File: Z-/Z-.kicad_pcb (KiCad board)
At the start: 4 copper layers, 98 x 98 mm, 138 parts, among them J1 200528-0100, J2 Conn_Coaxial, J3 Conn_Coaxial, J4 200528-0100, J5 Conn_01x02, K1 IM02DGR, Q1 NX3008NBKS, Q10 NX3008NBKS, Q11 IRLML2803, Q12 MBT2222ADW1T1, Q13 IRLML2803, Q14 NX3008NBKS, Q15 IRF7404, Q16 MBT2222ADW1T1, Q17 IRF7404, Q18 IRLML2803, Q19 IRF7404, Q2 NX3008NBKS, Q3 MBT2222ADW1T1, Q4 MBT2222ADW1T1, Q5 NX3008NBKS, Q6 NX3008NBKS, Q7 MBT2222ADW1T1, Q8 MBT2222ADW1T1, Q9 MMBT2222AT, U1 OPT4003DNPRQ1, U2 LTC4316xDD, U3 ADM1176-1ARMZ-R7, U4 NCV891330PD50R2G, U5 DRV8830DRC

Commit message: Moved things around
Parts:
- moved Q15 98.6 mm to (206.3, 52.5)
- moved Q17 98.6 mm to (219.8, 52.5)
- moved Q11 98.6 mm to (204.4, 58.5)
- moved Q18 98.6 mm to (211.1, 58.5)
- moved Q19 98.6 mm to (213.0, 52.5)
- moved R56 98.6 mm to (214.4, 60.6)
- moved R59 98.6 mm to (214.4, 59.0)
- moved R60 98.6 mm to (214.4, 57.4)
- moved Q13 98.6 mm to (217.8, 58.5)
- moved R39 98.6 mm to (207.7, 60.6)
- moved R41 98.6 mm to (207.7, 59.0)
- moved R43 98.6 mm to (207.7, 57.3)
- moved R49 98.6 mm to (221.1, 60.6)
- moved R51 98.6 mm to (221.1, 59.0)
- moved R53 98.6 mm to (221.1, 57.4)
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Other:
- board text added: "SUN SENSOR"

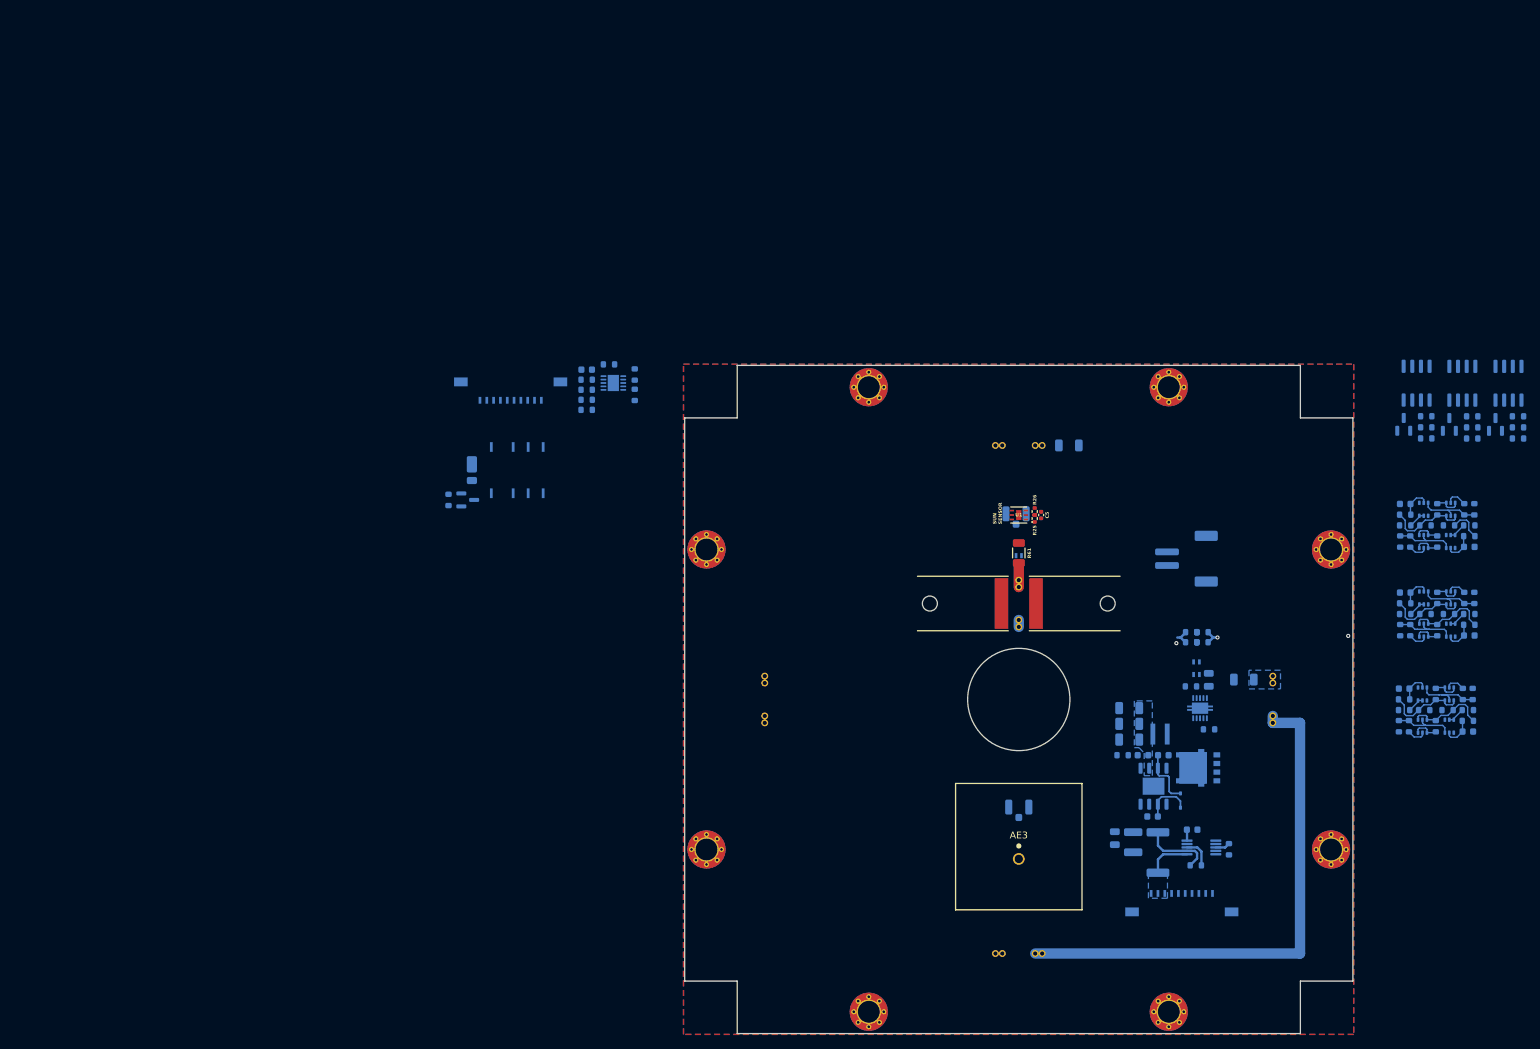
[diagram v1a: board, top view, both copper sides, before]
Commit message: Reworked board layout
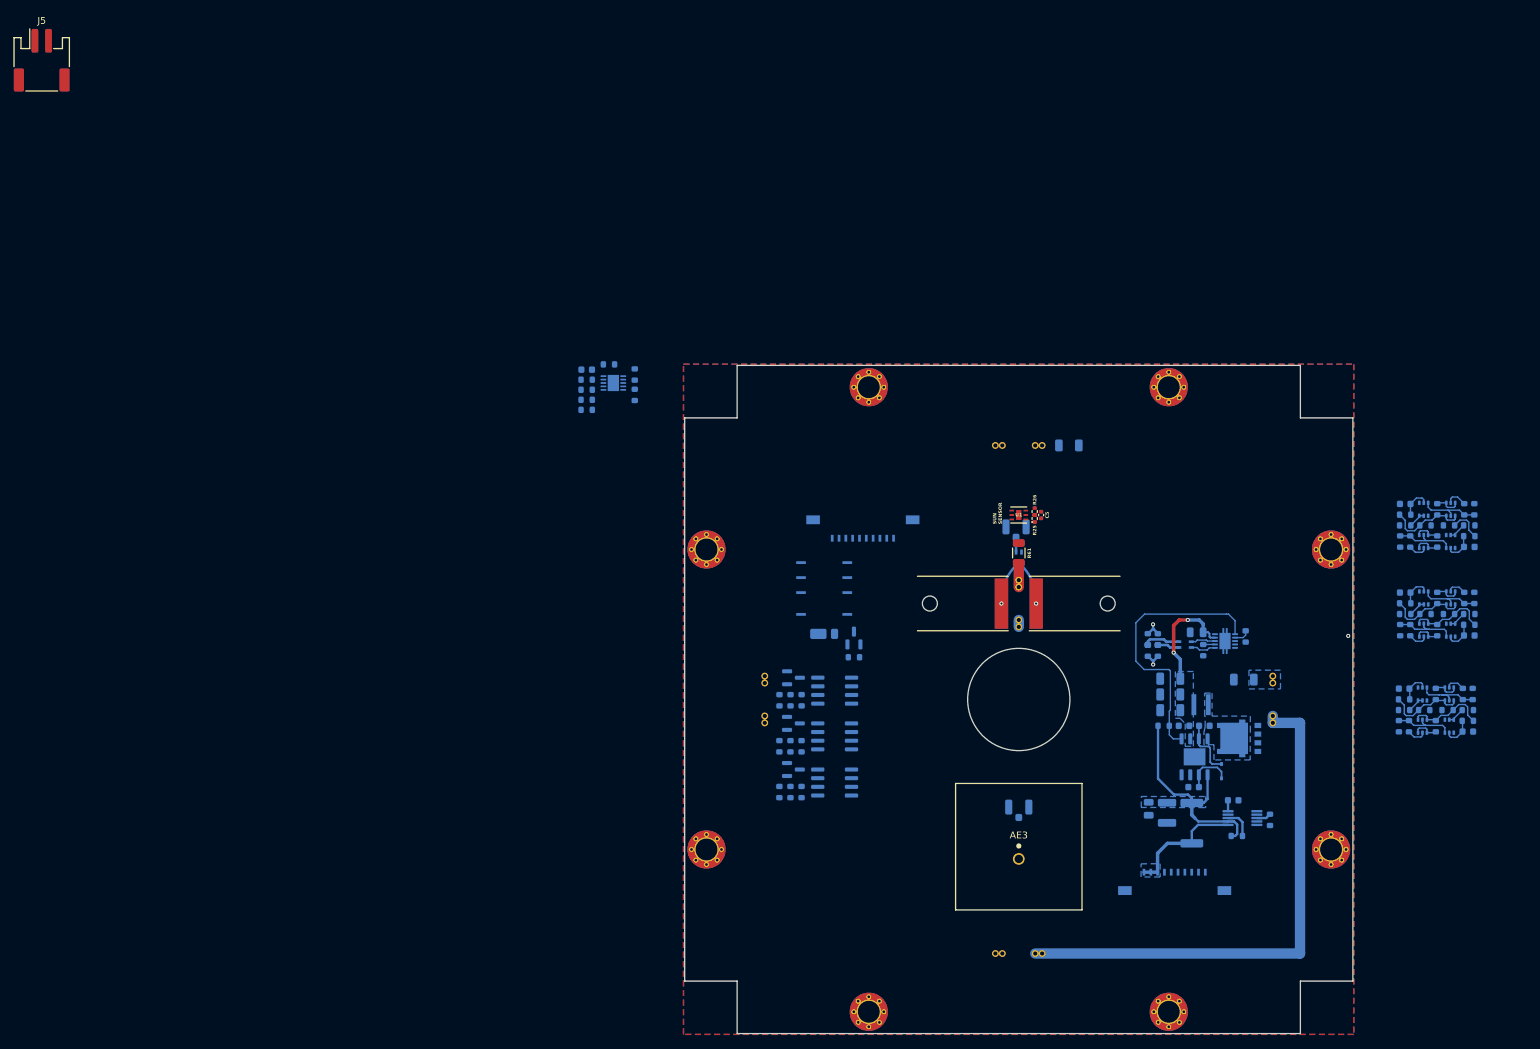
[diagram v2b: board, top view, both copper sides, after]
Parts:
- J5: moved to F.Cu
- moved J5 183.1 mm to (4.62, 5.12), turned to 0 degrees
- moved R49 120.1 mm to (112.8, 112.5), turned to -90 degrees
- moved R51 119.4 mm to (114.4, 112.5), turned to -90 degrees
- moved R53 118.7 mm to (116.1, 112.5), turned to -90 degrees
- moved Q17 114.9 mm to (120.9, 111.1), turned to 0 degrees
- moved Q13 114.7 mm to (114.9, 109.2), turned to 0 degrees
- moved R56 111.2 mm to (112.8, 105.7), turned to -90 degrees
- moved R59 110.4 mm to (114.4, 105.7), turned to -90 degrees
- moved R60 109.6 mm to (116.1, 105.7), turned to -90 degrees
- moved Q18 105.7 mm to (114.9, 102.4), turned to 0 degrees
- moved Q19 105.6 mm to (120.9, 104.3), turned to 0 degrees
- moved R39 102.3 mm to (112.8, 99.0), turned to -90 degrees
- moved R41 101.5 mm to (114.5, 99.0), turned to -90 degrees
- moved R43 100.6 mm to (116.1, 99.0), turned to -90 degrees
- moved Q11 96.9 mm to (114.9, 95.7), turned to 0 degrees
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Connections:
- net Net-(D2-K) renamed /I2C Devices/SW
- J4 pad 2: BURN_RELAY_A -> GND
- J4 pad 3: BURN_EN1 -> GND
- J4 pad 4: BURN_EN2 -> GND
- J4 pad 5: BURN_EN3 -> BURN_EN4
- J4 pad 6: BURN_EN4 -> BURN_EN3
- J4 pad 7: GND -> BURN_EN2
- J4 pad 8: GND -> BURN_EN1
- J4 pad 9: GND -> BURN_RELAY_A
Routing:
- net M_FAULT: track 0.00 -> 40.2 mm
- net VDRIVE: track 10.4 -> 32.2 mm
- net +5V: track 0.00 -> 16.7 mm, vias 0 -> 2
- net VBATT: track 6.53 -> 17.9 mm
- net Net-(AE2-Pad1): track 0.00 -> 6.14 mm, vias 0 -> 1
- net Net-(AE1-Pad1): track 0.00 -> 6.14 mm, vias 0 -> 1
- net COIL_P: track 0.00 -> 5.31 mm
- net /coil: track 23626.6 -> 23622.5 mm
- net Net-(U5-OUT2): track 0.00 -> 3.74 mm
- net Net-(U5-OUT1): track 0.00 -> 3.62 mm
- net COIL_N: track 0.00 -> 3.21 mm
- net Net-(U5-A0): track 0.00 -> 2.33 mm
- net Net-(J2-In): track 0.00 -> 2.17 mm
- net Net-(U5-ISENSE): track 0.00 -> 1.72 mm
- added copper zone on B.Cu, net /I2C Devices/SW
- added copper zone on B.Cu, net VDRIVE

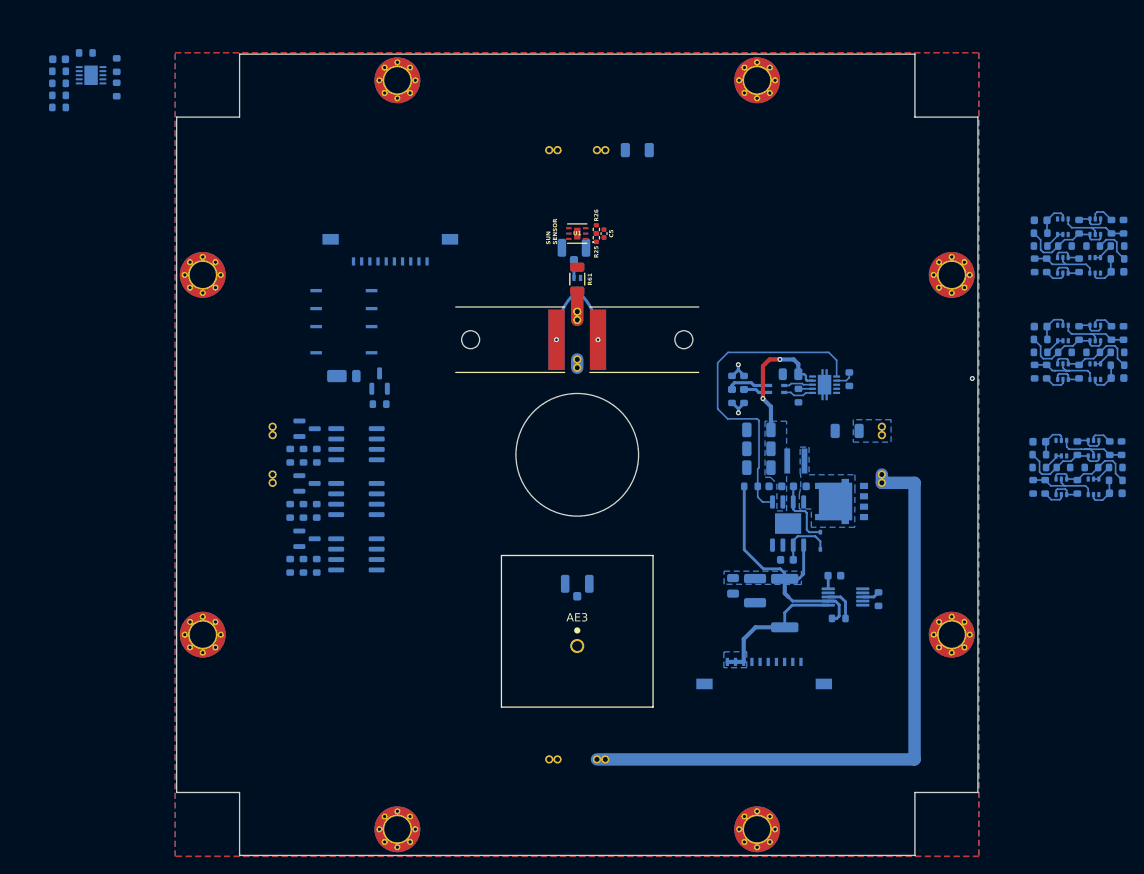
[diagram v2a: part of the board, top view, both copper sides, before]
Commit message: More layout updates
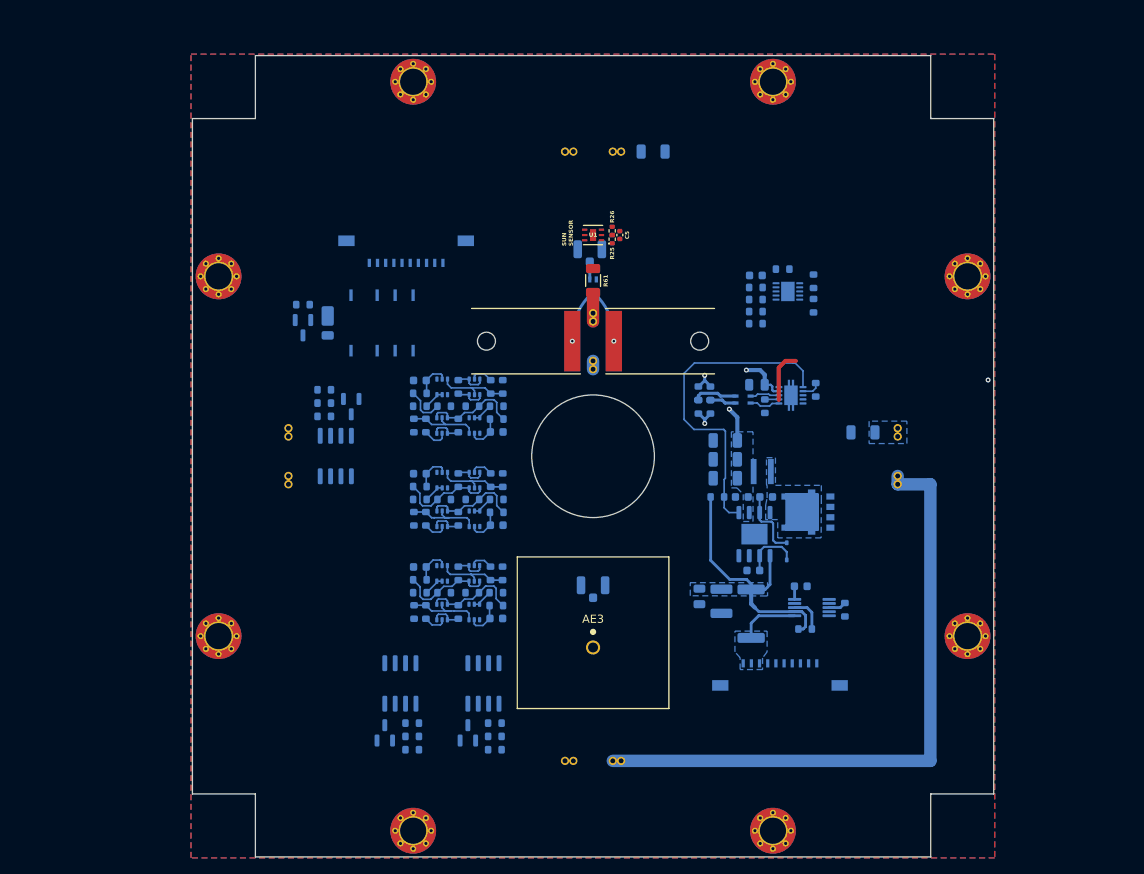
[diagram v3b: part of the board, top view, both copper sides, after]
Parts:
- moved R17 90.1 mm to (127.9, 95.3), turned to 90 degrees
- moved R63 89.2 mm to (176.8, 77.7)
- moved R64 89.2 mm to (176.8, 80.6)
- moved C17 89.2 mm to (169.8, 76.9)
- moved R62 89.2 mm to (173.0, 76.2)
- moved R65 89.2 mm to (169.8, 78.4)
- moved R66 89.2 mm to (169.8, 79.9)
- moved R67 89.2 mm to (169.8, 81.4)
- moved R68 89.2 mm to (169.8, 82.8)
- moved U2 89.2 mm to (173.7, 78.9)
- moved R54 88.8 mm to (128.0, 118.1), turned to 90 degrees
- moved R27 87.5 mm to (128.7, 92.9), turned to 0 degrees
- moved R1 87.3 mm to (129.4, 95.3), turned to 90 degrees
- moved R32 86.9 mm to (128.7, 91.4), turned to 0 degrees
- moved R40 86.5 mm to (128.7, 115.7), turned to 0 degrees
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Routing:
- net VBATT: track 17.9 -> 7.49 mm

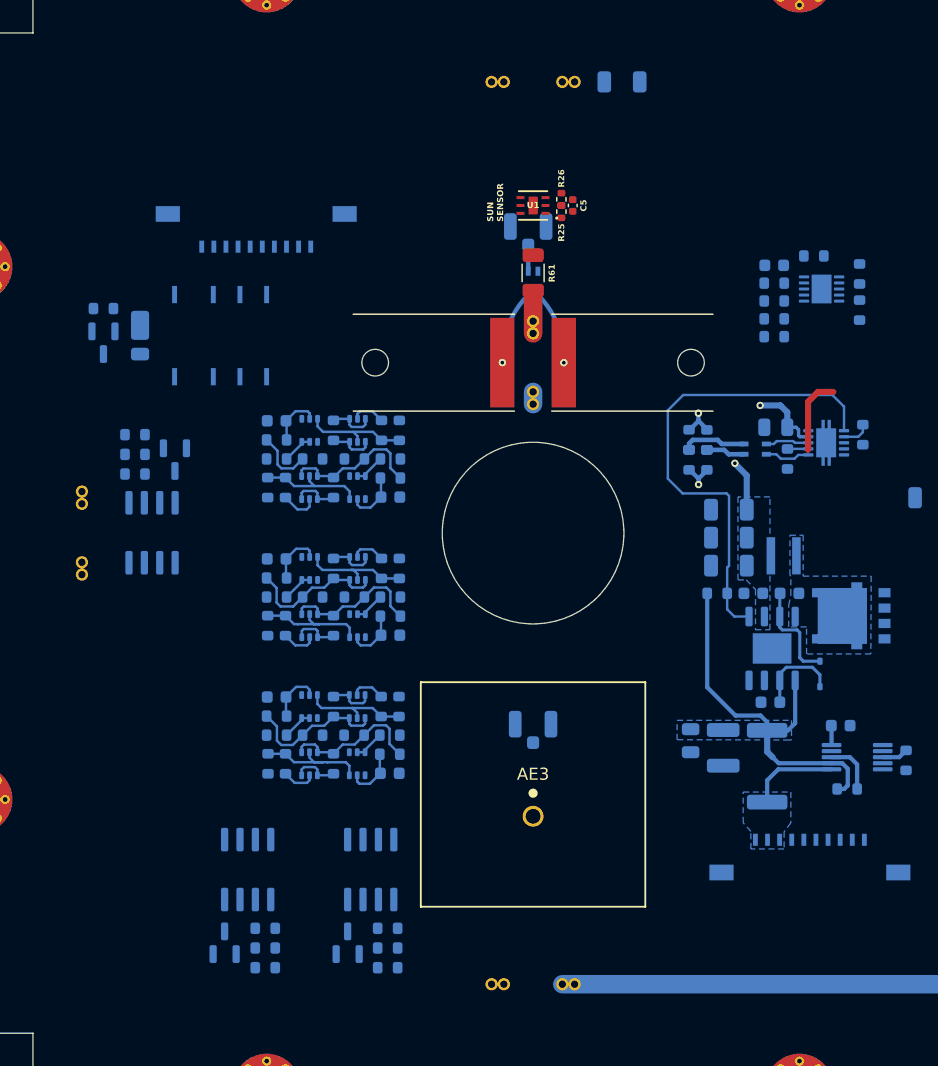
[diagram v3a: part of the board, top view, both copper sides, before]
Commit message: Power routing
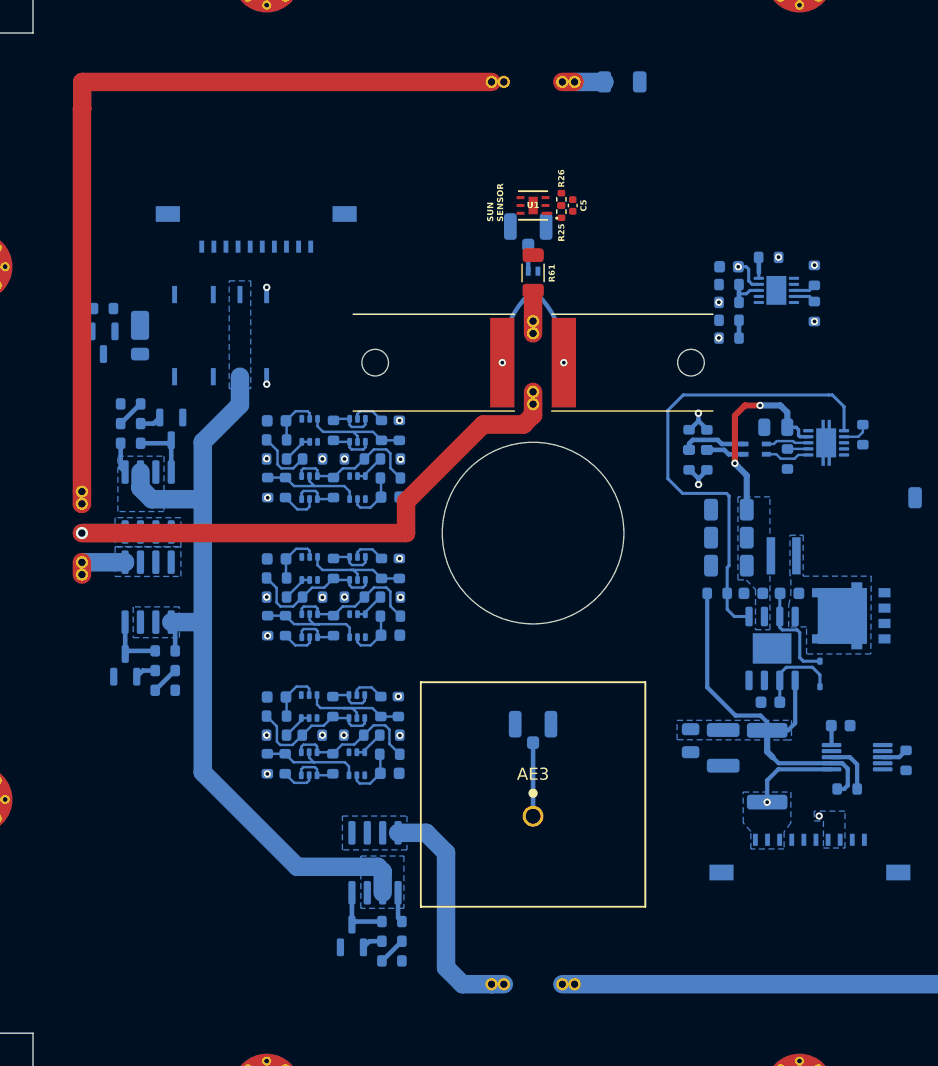
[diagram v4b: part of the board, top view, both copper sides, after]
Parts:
- moved R56 47.9 mm to (116.6, 88.4), turned to 180 degrees
- moved R59 44.7 mm to (116.6, 90.0), turned to 180 degrees
- moved Q18 42.7 mm to (120.0, 90.5), turned to -90 degrees
- moved R60 41.6 mm to (116.6, 91.6), turned to 180 degrees
- moved Q19 31.4 mm to (118.1, 96.5), turned to -90 degrees
- moved R39 21.3 mm to (119.5, 112.0), turned to 0 degrees
- moved R41 18.0 mm to (119.5, 110.4), turned to 0 degrees
- moved Q11 17.5 mm to (116.2, 110.0), turned to 90 degrees
- moved R43 14.8 mm to (119.5, 108.8), turned to 0 degrees
- moved R42 11.9 mm to (127.9, 118.1), turned to 90 degrees
- moved R54 11.8 mm to (138.7, 113.4), turned to -90 degrees
- moved C18 11.3 mm to (128.7, 112.6), turned to 180 degrees
- moved C16 11.3 mm to (138.0, 118.9), turned to 0 degrees
- moved R58 9.87 mm to (128.7, 114.2), turned to 0 degrees
- moved R46 9.86 mm to (138.0, 117.3), turned to 180 degrees
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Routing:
- net VBATT: track 7.49 -> 94.0 mm, vias 0 -> 3
- net 3.3V: track 0.00 -> 75.8 mm, vias 0 -> 25
- net /Burn Wires/VBURN_A_IN: track 0.00 -> 71.0 mm
- net Net-(JP1-Pad2): track 0.00 -> 68.7 mm
- net /Burn Wires/VBURN3: track 1.02 -> 48.3 mm, vias 0 -> 1
- net /Burn Wires/VBURN2: track 0.00 -> 19.5 mm
- net /coil: track 23622.5 -> 23635.7 mm
- net Net-(AE3-A): track 0.00 -> 6.08 mm
- net Net-(Q18-D): track 0.00 -> 5.26 mm
- net Net-(Q11-D): track 0.00 -> 5.22 mm
- net Net-(Q13-D): track 0.00 -> 5.21 mm
- net /Burn Wires/VBURN1: track 0.00 -> 4.58 mm
- net Net-(JP4-Pad2): track 0.00 -> 3.47 mm
- net Net-(U2-XORL): track 0.00 -> 3.23 mm
- net BURN_EN1: track 0.00 -> 2.32 mm
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- added copper zone on B.Cu, net /Burn Wires/VBURN1
- added copper zone on B.Cu, net /Burn Wires/VBURN2
- added copper zone on B.Cu, net /Burn Wires/VBURN3
- added copper zone on B.Cu, net /Burn Wires/VBURN_A_IN
- added copper zone on B.Cu, net 3.3V
- added copper zone on In1.Cu, net 3.3V
- added copper zone on In1.Cu, net GND
